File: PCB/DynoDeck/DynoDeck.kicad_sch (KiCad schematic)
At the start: 70 parts, among them J1 USB_C_Receptacle_USB2.0_16P, J2 E-paper, J3 CardKB, J4 PGRM, J5 u.FL, J6 SMA, SW1 QON, SW2 RESET, SW3 SW_SPDT, U1 E73-2G4M08S1C, U2 SX1262IMLTRT, U3 BQ25895RTW, U5 BGS12WN6E6327, U6 USBLC6-2SC6, U7 TUSB320, U8 BGS12WN6E6327, U9 MD7218E33PC1, Y1 32.768kHz, Y2 OW7EL89CENUXK7YLC-32M

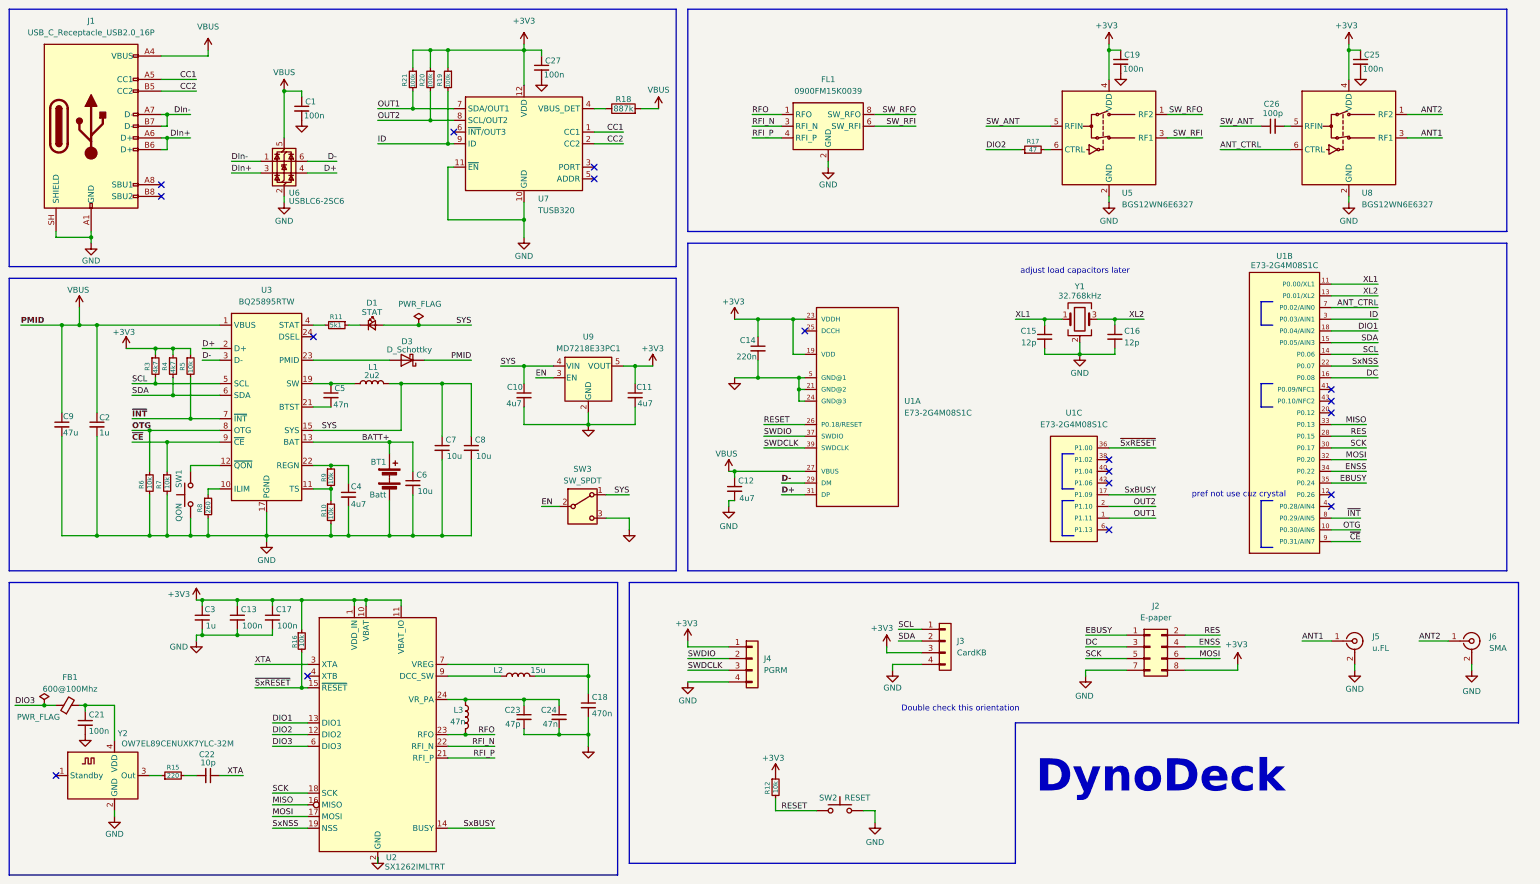
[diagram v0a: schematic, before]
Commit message: partial footprints
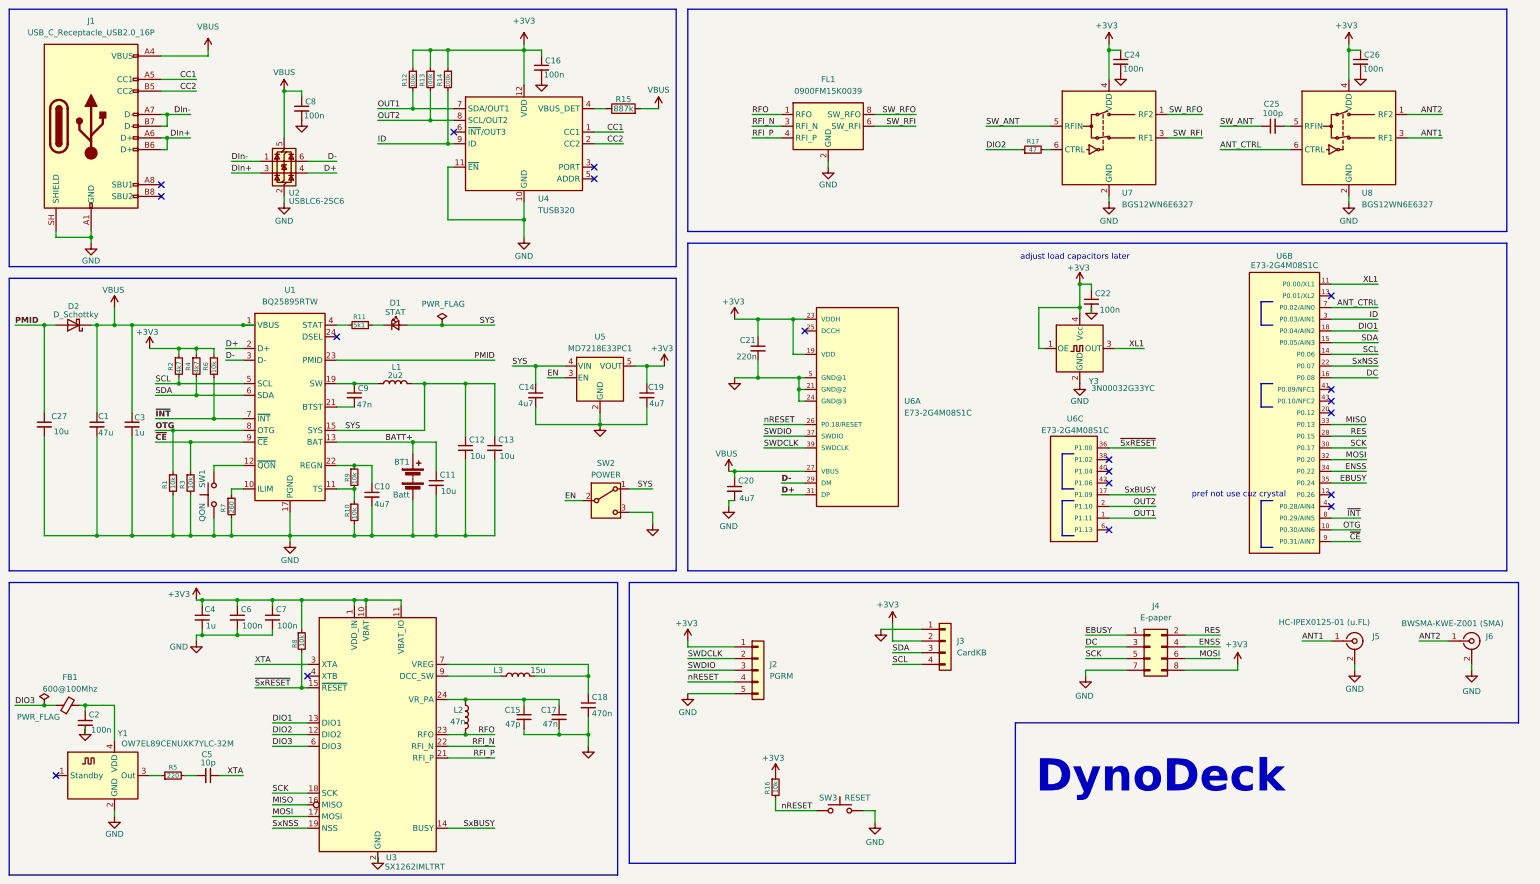
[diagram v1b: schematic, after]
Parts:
- removed C15, C16: 12p, symbol Device:C_Small
- removed J4: PGRM, symbol Connector_Generic:Conn_01x04
- removed Y1: 32.768kHz, symbol Device:Crystal_GND24
- added C22: 100n, Capacitor_SMD:C_0603_1608Metric, symbol Device:C_Small
- added C27: 10u, Capacitor_SMD:C_0603_1608Metric, symbol Device:C_Small
- added J2: PGRM, PGRMPins:PogoPin_1x05_P2.54mm_Pad1.8mm, symbol Connector_Generic:Conn_01x05
- added Y3: 3N00032G33YC, Oscillator:Oscillator_SMD_Abracon_ASE-4Pin_3.2x2.5mm_HandSoldering, symbol Oscillator:SG-210SDD
- BT1: footprint (none) -> Connector_JST:JST_PH_S2B-PH-K_1x02_P2.00mm_Horizontal
- C1: renamed from C9; footprint (none) -> Capacitor_SMD:C_0603_1608Metric
- C10: renamed from C4; footprint (none) -> Capacitor_SMD:C_0603_1608Metric
- C11: renamed from C6; footprint (none) -> Capacitor_SMD:C_0603_1608Metric
- C12: renamed from C7; footprint (none) -> Capacitor_SMD:C_0603_1608Metric
- C13: renamed from C8; footprint (none) -> Capacitor_SMD:C_0603_1608Metric
- C14: renamed from C10; footprint (none) -> Capacitor_SMD:C_0603_1608Metric
- C15: renamed from C23; footprint (none) -> Capacitor_SMD:C_0603_1608Metric
- C16: renamed from C27; footprint (none) -> Capacitor_SMD:C_0603_1608Metric
- C17: renamed from C24; footprint (none) -> Capacitor_SMD:C_0603_1608Metric
- C18: footprint (none) -> Capacitor_SMD:C_0603_1608Metric
- C19: renamed from C11; footprint (none) -> Capacitor_SMD:C_0603_1608Metric
- C2: renamed from C21; footprint (none) -> Capacitor_SMD:C_0603_1608Metric
- C20: renamed from C12; footprint (none) -> Capacitor_SMD:C_0603_1608Metric
- C21: renamed from C14; footprint (none) -> Capacitor_SMD:C_0603_1608Metric
- C24: renamed from C19; footprint (none) -> Capacitor_SMD:C_0603_1608Metric
- C25: renamed from C26; footprint (none) -> Capacitor_SMD:C_0402_1005Metric
- C26: renamed from C25; footprint (none) -> Capacitor_SMD:C_0603_1608Metric
- C3: renamed from C2; footprint (none) -> Capacitor_SMD:C_0603_1608Metric
- C4: renamed from C3; footprint (none) -> Capacitor_SMD:C_0603_1608Metric
- C5: renamed from C22; footprint (none) -> Capacitor_SMD:C_0603_1608Metric
- C6: renamed from C13; footprint (none) -> Capacitor_SMD:C_0603_1608Metric
- C7: renamed from C17; footprint (none) -> Capacitor_SMD:C_0603_1608Metric
- C8: renamed from C1; footprint (none) -> Capacitor_SMD:C_0603_1608Metric
- C9: renamed from C5; footprint (none) -> Capacitor_SMD:C_0603_1608Metric
- D1: footprint (none) -> LED_SMD:LED_0603_1608Metric
- FB1: footprint (none) -> Inductor_SMD:L_0603_1608Metric_Pad1.05x0.95mm_HandSolder
- J3: footprint (none) -> Connector_JST:JST_PH_S4B-PH-K_1x04_P2.00mm_Horizontal
- J5: value u.FL -> HC-IPEX0125-01 (u.FL); footprint (none) -> Connector_Coaxial:U.FL_Molex_MCRF_73412-0110_Vertical
- J6: value SMA -> BWSMA-KWE-Z001 (SMA); footprint (none) -> Connector_Coaxial:SMA_BAT_Wireless_BWSMA-KWE-Z001
- L3: renamed from L2; footprint (none) -> Inductor_SMD:L_Sunlord_MWSA0503S
- R1: renamed from R6; footprint (none) -> Resistor_SMD:R_0603_1608Metric
- R10, R11, R17, R4, R9: footprint (none) -> Resistor_SMD:R_0603_1608Metric
- R12: renamed from R21; footprint (none) -> Resistor_SMD:R_0603_1608Metric
- R13: renamed from R20; footprint (none) -> Resistor_SMD:R_0603_1608Metric
- R14: renamed from R19; footprint (none) -> Resistor_SMD:R_0603_1608Metric
- R15: renamed from R18; footprint (none) -> Resistor_SMD:R_0603_1608Metric
- R16: renamed from R12; footprint (none) -> Resistor_SMD:R_0603_1608Metric
- R2: renamed from R3; footprint (none) -> Resistor_SMD:R_0603_1608Metric
- R3: renamed from R7; footprint (none) -> Resistor_SMD:R_0603_1608Metric
- R5: renamed from R15; footprint (none) -> Resistor_SMD:R_0603_1608Metric
- R6: renamed from R5; footprint (none) -> Resistor_SMD:R_0603_1608Metric
- R7: renamed from R8; footprint (none) -> Resistor_SMD:R_0603_1608Metric
- R8: renamed from R16; footprint (none) -> Resistor_SMD:R_0603_1608Metric
- SW2: renamed from SW3; value SW_SPDT -> POWER
- renumbered D3 to D2, J2 to J4, L3 to L2, SW2 to SW3, U3 to U1, U6 to U2, U2 to U3, U7 to U4, U9 to U5, U1 to U6, U5 to U7, Y2 to Y1
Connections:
- net +3V3: now also J3.2 (Pin_2), C22.1, J2.1 (Pin_1), Y3.1 (OE), Y3.4 (Vcc); no longer J3.3 (Pin_3)
- net GND: now also J3.1 (Pin_1), C22.2, C27.2, J2.5 (Pin_5), Y3.2 (GND); no longer J3.4 (Pin_4)
- net SCL: now also J3.4 (Pin_4); no longer J3.1 (Pin_1)
- net SDA: now also J3.3 (Pin_3); no longer J3.2 (Pin_2)
- net SWDCLK: now also J2.2 (Pin_2)
- net SWDIO: now also J2.3 (Pin_3)
- net XL1: now also Y3.3 (OUT)
- net PMID: now reaches D2.2 (A), U1.23 (PMID)
- net PMID: now also C27.1
- net RESET renamed nRESET
- net nRESET: now also J2.4 (Pin_4)
- net XL2: no longer names the net of U6.13 (P0.01/XL2)
- no-connect marks 18 -> 19
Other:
- note removed: "Double check this orientation"
- moved on the sheet: BT1, C1, C10, C11, C12, C13, C14, C19, C3, C9, D1, D2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

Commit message: Footprints
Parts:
- added R18: 10k, Resistor_SMD:R_0603_1608Metric, symbol Device:R_Small
- added R19: 100k, Resistor_SMD:R_0603_1608Metric, symbol Device:R_Small
- added SW4: IO1, Button_Switch_SMD:SW_SPST_PTS647_Sx38, symbol Switch:SW_Push
- D2: footprint (none) -> Diode_SMD:D_SMB
- L1: footprint (none) -> Inductor_SMD:L_Sunlord_MWSA0503S
- L2: footprint (none) -> Inductor_SMD:L_1008_2520Metric
- SW1, SW3: footprint (none) -> Button_Switch_SMD:SW_SPST_TS-1088-xR020
- SW2: footprint (none) -> Button_Switch_SMD:SW_SPDT_CK_JS102011SAQN
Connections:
- net +3V3: now also R18.1
- net EN: now also R19.1
- net GND: now also R19.2, SW4.2
- net ~{SxRESET}: now also U6.38 (P1.02); no longer U6.36 (P1.00)
- new net USER1: R18.2, SW4.1, U6.36 (P1.00)
- no-connect marks 19 -> 18
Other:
- moved on the sheet: C8, R16, SW3

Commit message: Footprints
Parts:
- added J7: CardKBRef, CardKBRef:CardKBRef, symbol Connector_Generic:Conn_01x04
- J3: value CardKB -> CardKBConn
- J4: footprint Connector_PinSocket_2.54mm:PinSocket_2x04_P2.54mm_Vertical -> WeActStudio:weact_epaper_29
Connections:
- no-connect marks 18 -> 22
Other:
- note removed: "adjust load capacitors later"
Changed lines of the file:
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@@
 		)
 	)
-	(text "adjust load capacitors later"
-		(exclude_from_sim no)
-		(at 246.634 69.088 0)
-		(effects
-			(font
-				(size 1.27 1.27)
-			)
-		)
-	)
 	(junction
 		(at 34.29 83.82)
@@
 	)
 	(no_connect
+		(at 213.36 170.18)
+	)
+	(no_connect
 		(at 142.24 52.07)
 	)
@@
 	)
 	(no_connect
+		(at 213.36 172.72)
+	)
+	(no_connect
 		(at 254 118.11)
 	)
@@
 	)
 	(no_connect
+		(at 213.36 167.64)
+	)
+	(no_connect
 		(at 142.24 49.53)
 	)
 	(no_connect
+		(at 213.36 165.1)
+	)
+	(no_connect
 		(at 111.76 41.91)
 	)
@@
 			)
 		)
-		(property "Footprint" "Connector_PinSocket_2.54mm:PinSocket_2x04_P2.54mm_Vertical"
+		(property "Footprint" "WeActStudio:weact_epaper_29"
 			(at 262.89 153.67 0)
 			(hide yes)
@@
 	)
 	(symbol
+		(lib_id "Connector_Generic:Conn_01x04")
+		(at 218.44 167.64 0)
+		(unit 1)
+		(body_style 1)
+		(exclude_from_sim no)
+		(in_bom yes)
+		(on_board yes)
+		(in_pos_files yes)
+		(dnp no)
+		(fields_autoplaced yes)
+		(property "Reference" "J7"
+			(at 220.98 167.6399 0)
+			(show_name no)
+			(do_not_autoplace no)
+			(effects
+				(font
+					(size 1.27 1.27)
+				)
+				(justify left)
+			)
+		)
+		(property "Value" "CardKBRef"
+			(at 220.98 170.1799 0)
+			(show_name no)
+			(do_not_autoplace no)
+			(effects
+				(font
+					(size 1.27 1.27)
+				)
+				(justify left)
+			)
+		)
+		(property "Footprint" "CardKBRef:CardKBRef"
+			(at 218.44 167.64 0)
+			(hide yes)
+			(show_name no)
+			(do_not_autoplace no)
+			(effects
+				(font
+					(size 1.27 1.27)
+				)
+			)
+		)
+		(property "Datasheet" ""
+			(at 218.44 167.64 0)
+			(hide yes)
+			(show_name no)
+			(do_not_autoplace no)
+			(effects
+				(font
+					(size 1.27 1.27)
+				)
+			)
+		)
+		(property "Description" "Generic connector, single row, 01x04, script generated (kicad-library-utils/schlib/autogen/connector/)"
+			(at 218.44 167.64 0)
+			(hide yes)
+			(show_name no)
+			(do_not_autoplace no)
+			(effects
+				(font
+					(size 1.27 1.27)
+				)
+			)
+		)
+		(pin "4"
+		)
+		(pin "3"
+		)
+		(pin "2"
+		)
+		(pin "1"
+		)
+		(instances
+			(project "DynoDeck"
+				(path "/d751e66f-06ea-4bc9-898a-20a2be86c932"
+					(reference "J7")
+					(unit 1)
+				)
+			)
+		)
+	)
+	(symbol
 		(lib_id "power:VBUS")
 		(at 38.1 81.28 0)
@@
 			)
 		)
-		(property "Value" "CardKB"
+		(property "Value" "CardKBConn"
 			(at 220.98 154.9399 0)
 			(show_name no)

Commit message: rough layout
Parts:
- removed U7, U8: BGS12WN6E6327, Package_LGA:Infineon_PG-TSNP-6-10_0.7x1.1mm_0.7x1.1mm_P0.4mm, symbol RF_Switch:BGS12WN6E6327
- added H1: MountBTML, MountingHole:MountingHole_2.7mm_M2.5, symbol Mechanical:MountingHole
- added H2: MountBTMR, MountingHole:MountingHole_2.7mm_M2.5, symbol Mechanical:MountingHole
- added U7, U8: PE42422MLAA-Z, PE42422:PE42422-QFN-12_L2.0-W2.0-P0.50-BL-EP, symbol PE42422:PE42422MLAA-Z
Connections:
- net +3V3: now also U7.12 (VDD), U8.11 (LS), U8.12 (VDD)
- net ANT1: now also U8.8 (RF1)
- net ANT2: now also U8.2 (RF2)
- net ANT_CTRL: now also U8.10 (V1)
- net GND: now also U7.1 (GND), U7.11 (LS), U7.13 (EP), U7.3 (GND), U7.4 (GND/NC), U7.6 (GND), U7.7 (GND), U7.9 (DGND), U8.1 (GND), U8.13 (EP), U8.3 (GND), U8.4 (GND/NC), U8.6 (GND), U8.7 (GND), U8.9 (DGND)
- net SW_RFI: now also U7.2 (RF2)
- net SW_RFO: now also U7.8 (RF1)
- net at C25.2: now also U8.5 (RFC)
- net at R17.2: now also U7.10 (V1)
- net SW_ANT renamed SW_RFIO
- net SW_RFIO: now also U7.5 (RFC)
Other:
- moved on the sheet: C25, J2, J3, J4, J5, J6, J7, R17, R18, SW4

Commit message: Power Circuit
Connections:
- net CC1: now also U4.2 (CC2); no longer U4.1 (CC1)
- net CC2: now also U4.1 (CC1); no longer U4.2 (CC2)
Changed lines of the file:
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@@
+	(wire
+		(pts
+			(xy 142.24 41.91) (xy 148.59 41.91)
+		)
+		(stroke
+			(width 0)
+			(type default)
+		)
+	)
 	(wire
 		(pts
@@
 	(wire
 		(pts
-			(xy 142.24 41.91) (xy 148.59 41.91)
-		)
-		(stroke
-			(width 0)
-			(type default)
-		)
-	)
-	(wire
-		(pts
 			(xy 58.42 24.13) (xy 58.42 25.4)
 		)
@@
 	(wire
 		(pts
+			(xy 142.24 44.45) (xy 148.59 44.45)
+		)
+		(stroke
+			(width 0)
+			(type default)
+		)
+	)
+	(wire
+		(pts
 			(xy 107.95 120.65) (xy 107.95 129.54)
 		)
@@
 		(pts
 			(xy 302.26 74.93) (xy 312.42 74.93)
-		)
-		(stroke
-			(width 0)
-			(type default)
-		)
-	)
-	(wire
-		(pts
-			(xy 142.24 44.45) (xy 148.59 44.45)
 		)
 		(stroke
@@
 	)
 	(label "CC1"
-		(at 148.59 41.91 180)
+		(at 148.59 44.45 180)
 		(effects
 			(font
@@
 	)
 	(label "CC2"
-		(at 148.59 44.45 180)
-		(effects
-			(font
+		(at 148.59 41.91 180)
+		(effects
+			(font

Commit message: Part of Sx1262
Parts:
- C24, C26: footprint Capacitor_SMD:C_0603_1608Metric -> Capacitor_SMD:C_0402_1005Metric
- FB1: footprint Inductor_SMD:L_0603_1608Metric_Pad1.05x0.95mm_HandSolder -> Inductor_SMD:L_0603_1608Metric
- L2: footprint Inductor_SMD:L_1008_2520Metric -> Inductor_SMD:L_0402_1005Metric
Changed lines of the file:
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@@
 			)
 		)
-		(property "Footprint" "Inductor_SMD:L_1008_2520Metric"
+		(property "Footprint" "Inductor_SMD:L_0402_1005Metric"
 			(at 114.3 168.91 0)
 			(hide yes)
@@
 			)
 		)
-		(property "Footprint" "Capacitor_SMD:C_0603_1608Metric"
+		(property "Footprint" "Capacitor_SMD:C_0402_1005Metric"
 			(at 256.54 26.67 0)
 			(hide yes)
@@
 			)
 		)
-		(property "Footprint" "Inductor_SMD:L_0603_1608Metric_Pad1.05x0.95mm_HandSolder"
+		(property "Footprint" "Inductor_SMD:L_0603_1608Metric"
 			(at 27.94 168.148 90)
 			(hide yes)
@@
 			)
 		)
-		(property "Footprint" "Capacitor_SMD:C_0603_1608Metric"
+		(property "Footprint" "Capacitor_SMD:C_0402_1005Metric"
 			(at 308.61 26.67 0)
 			(hide yes)
